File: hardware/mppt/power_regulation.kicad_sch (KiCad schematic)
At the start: 68 parts, among them IC1501 LMR38010SDDAR, IC1502 TPS2121, J1501 Conn_01x02, J1502 CT3151, J1503 CT3151, J1504 CT3151, U1501 AP63205WU, U1502 TLV75733PDBV

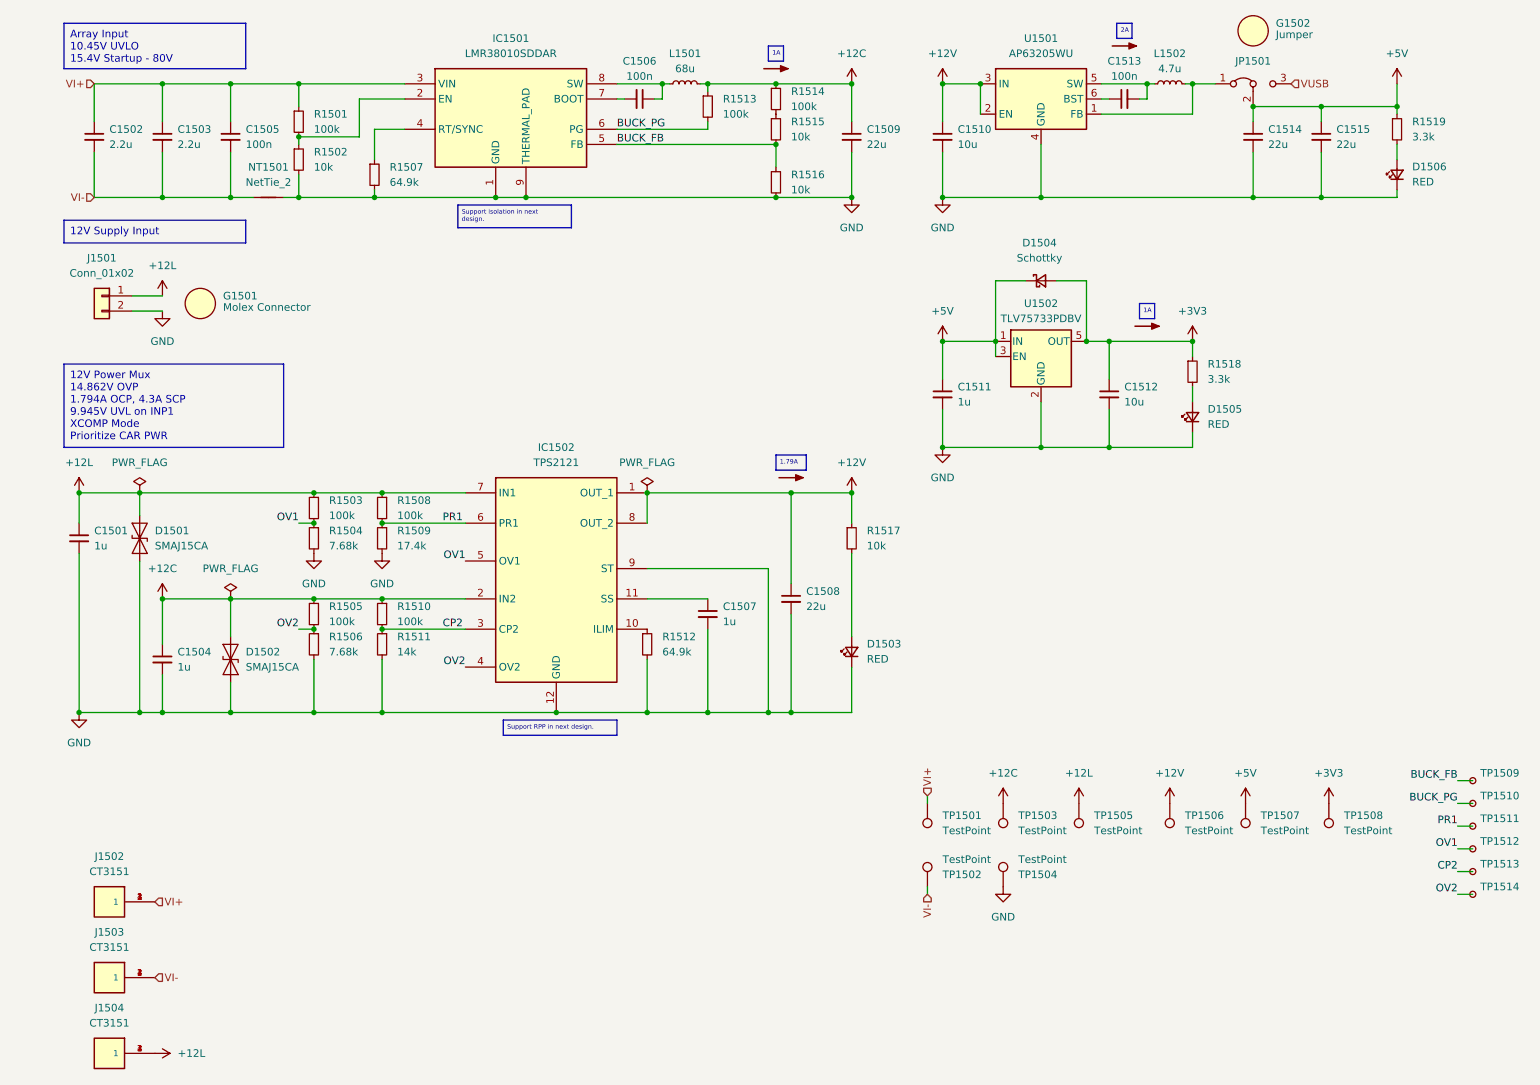
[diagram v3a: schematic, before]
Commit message: complete layout, drc, signaling optimizations and added dnp testpoints
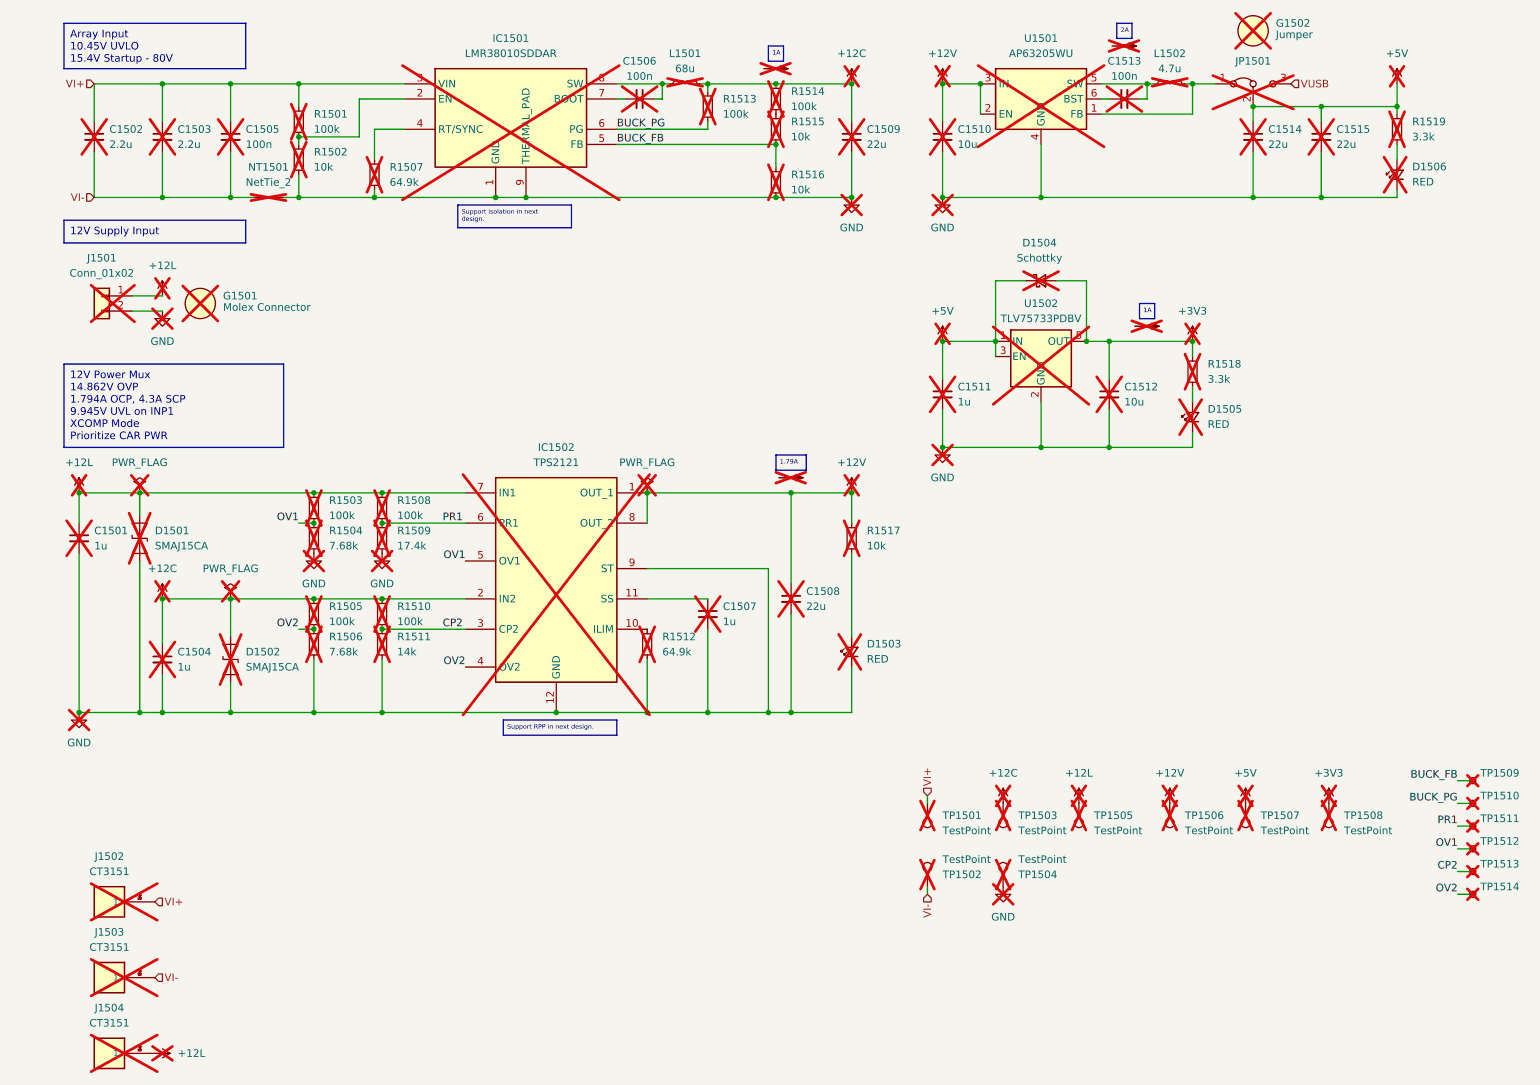
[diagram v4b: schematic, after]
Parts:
- C1501, C1502, C1503, C1504, C1505, C1506, C1507, C1508, C1509, C1510, C1511, C1512, C1513, C1514, C1515, D1501, D1502, D1503, D1504, D1505, D1506, G1501, G1502, IC1501, IC1502, J1501, J1502, J1503, J1504, L1501, L1502, R1501, R1502, R1503, R1504, R1505, R1506, R1507, R1508, R1509, R1510, R1511, R1512, R1513, R1514, R1515, R1516, R1517, R1518, R1519, TP1501, TP1502, TP1503, TP1504, TP1505, TP1506, TP1507, TP1508, TP1509, TP1510, TP1511, TP1512, TP1513, TP1514, U1501, U1502: now not fitted; now left out of the parts list
- JP1501, NT1501: now not fitted

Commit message: unset dnp for all components in sch
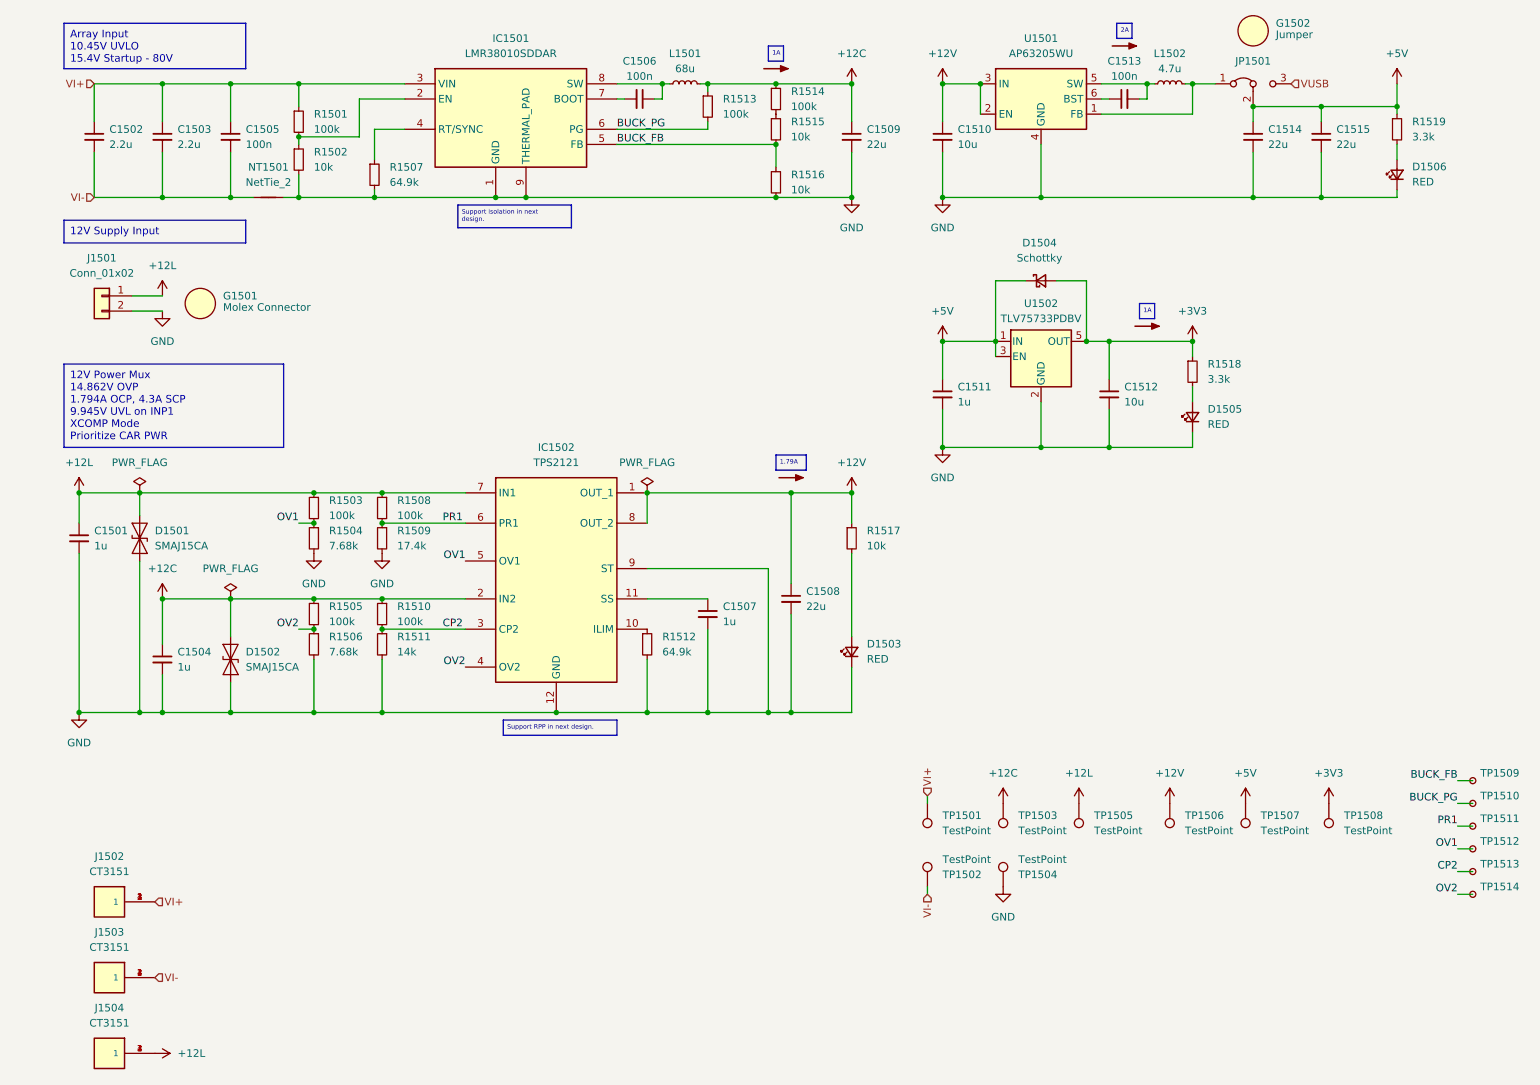
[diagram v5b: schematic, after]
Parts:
- C1501, C1502, C1503, C1504, C1505, C1506, C1507, C1508, C1509, C1510, C1511, C1512, C1513, C1514, C1515, D1501, D1502, D1503, D1504, D1505, D1506, G1501, G1502, IC1501, IC1502, J1501, J1502, J1503, J1504, JP1501, L1501, L1502, NT1501, R1501, R1502, R1503, R1504, R1505, R1506, R1507, R1508, R1509, R1510, R1511, R1512, R1513, R1514, R1515, R1516, R1517, R1518, R1519, TP1501, TP1502, TP1503, TP1504, TP1505, TP1506, TP1507, TP1508, TP1509, TP1510, TP1511, TP1512, TP1513, TP1514, U1501, U1502: now fitted; now in the parts list

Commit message: remove testpoints, integrat 60% of layout
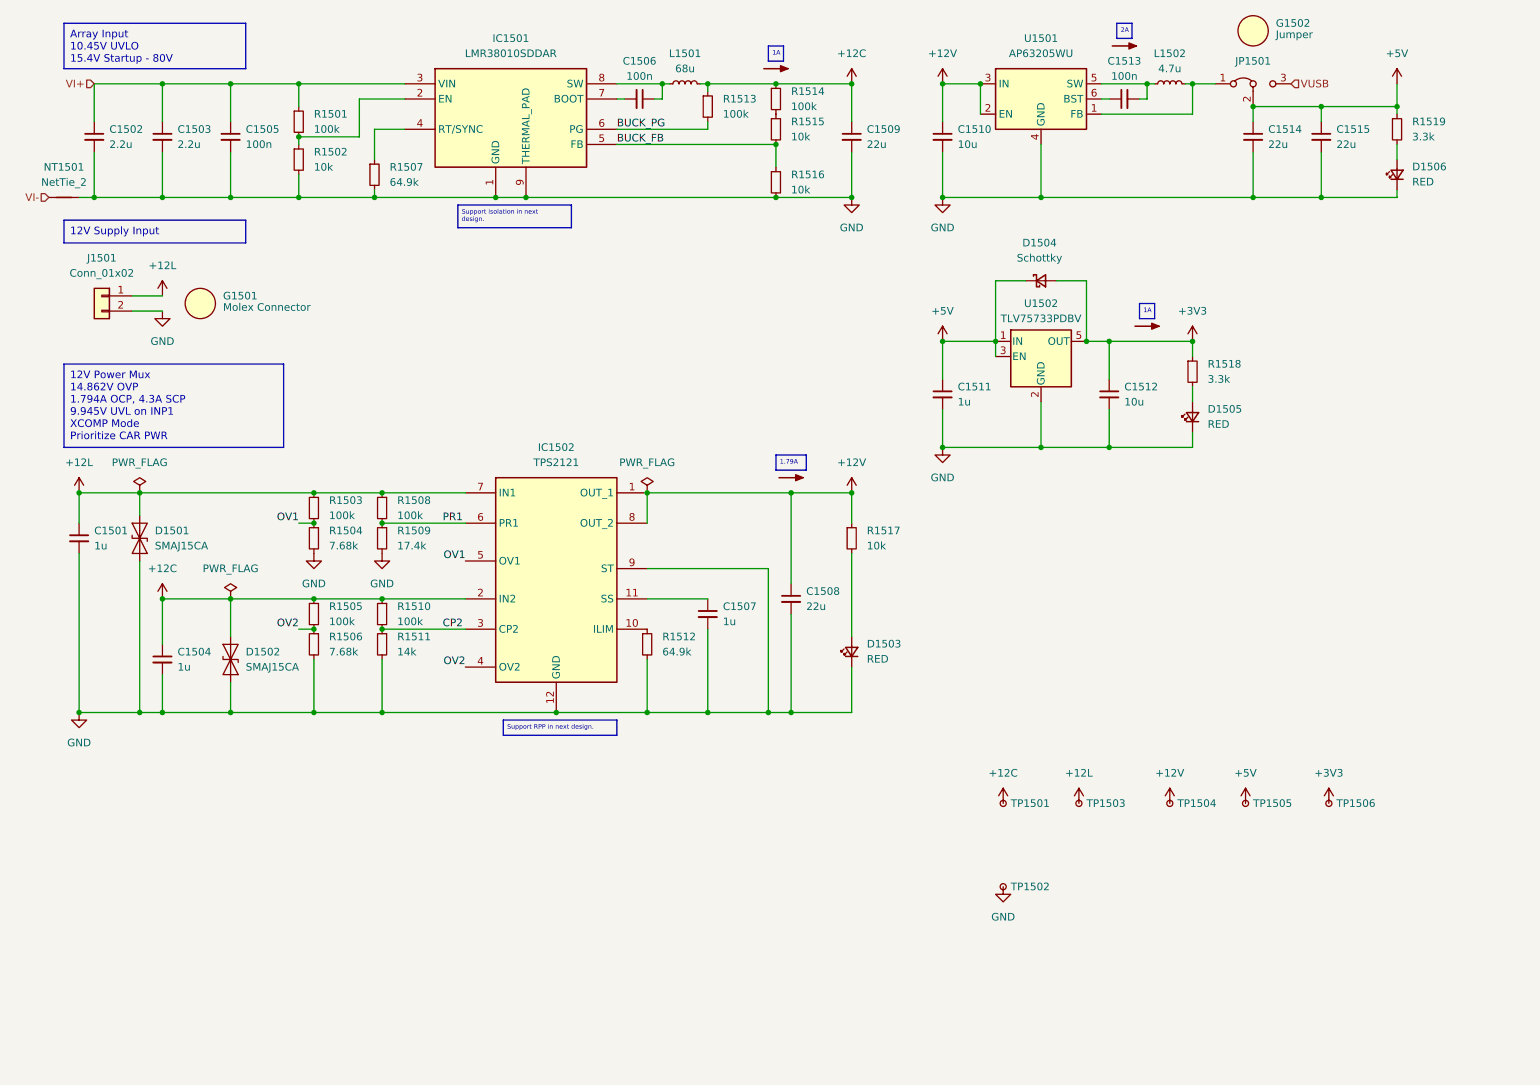
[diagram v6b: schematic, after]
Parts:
- removed J1502, J1503, J1504: CT3151, footprints:caltest_ct3151, symbol caltest_ct3151:CT3151
- removed TP1501, TP1502, TP1503, TP1504, TP1505, TP1506, TP1507, TP1508: TestPoint, TestPoint:TestPoint_Keystone_5000-5004_Miniature, symbol Connector:TestPoint
- removed TP1509, TP1510, TP1511, TP1512, TP1513, TP1514: TestPoint_Small, TestPoint:TestPoint_Pad_D1.0mm, symbol Connector:TestPoint_Small
- added TP1501, TP1502, TP1503, TP1504, TP1505, TP1506: TestPoint_Small, TestPoint:TestPoint_Pad_D1.0mm, symbol Connector:TestPoint_Small
- C1502, C1503: footprint Capacitor_SMD:C_2220_5750Metric_Pad1.97x5.40mm_HandSolder -> Capacitor_SMD:C_2220_5750Metric; Notes 150V Rating -> 200V Rating
- C1505: footprint Capacitor_SMD:C_1206_3216Metric_Pad1.33x1.80mm_HandSolder -> Capacitor_SMD:C_0805_2012Metric; Notes 85V Rating -> 200V Rating; P/N CGA5L3X7R2E104K160AA -> CGA4J3X7T2E104K125AA
- C1508, C1509, C1514, C1515: footprint Capacitor_SMD:C_1210_3225Metric_Pad1.33x2.70mm_HandSolder -> Capacitor_SMD:C_1206_3216Metric; P/N CGA6P3X7R1E226M250AB -> CGA5L1X5R1C226M160AC
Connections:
- net +12C: now also TP1501.1
- net +12L: now also TP1503.1
- net +12V: now also TP1504.1
- net +3V3: now also TP1506.1
- net +5V: now also TP1505.1
- net GND: now also C1502.2, C1503.2, C1505.2, TP1502.1
- net VI-: no longer C1502.2, C1503.2, C1505.2
